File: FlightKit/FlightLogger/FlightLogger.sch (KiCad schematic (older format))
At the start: 14 parts, among them P101 CONN_2, P102 CONN_9, P103 CONN_4, P104 CONN_4

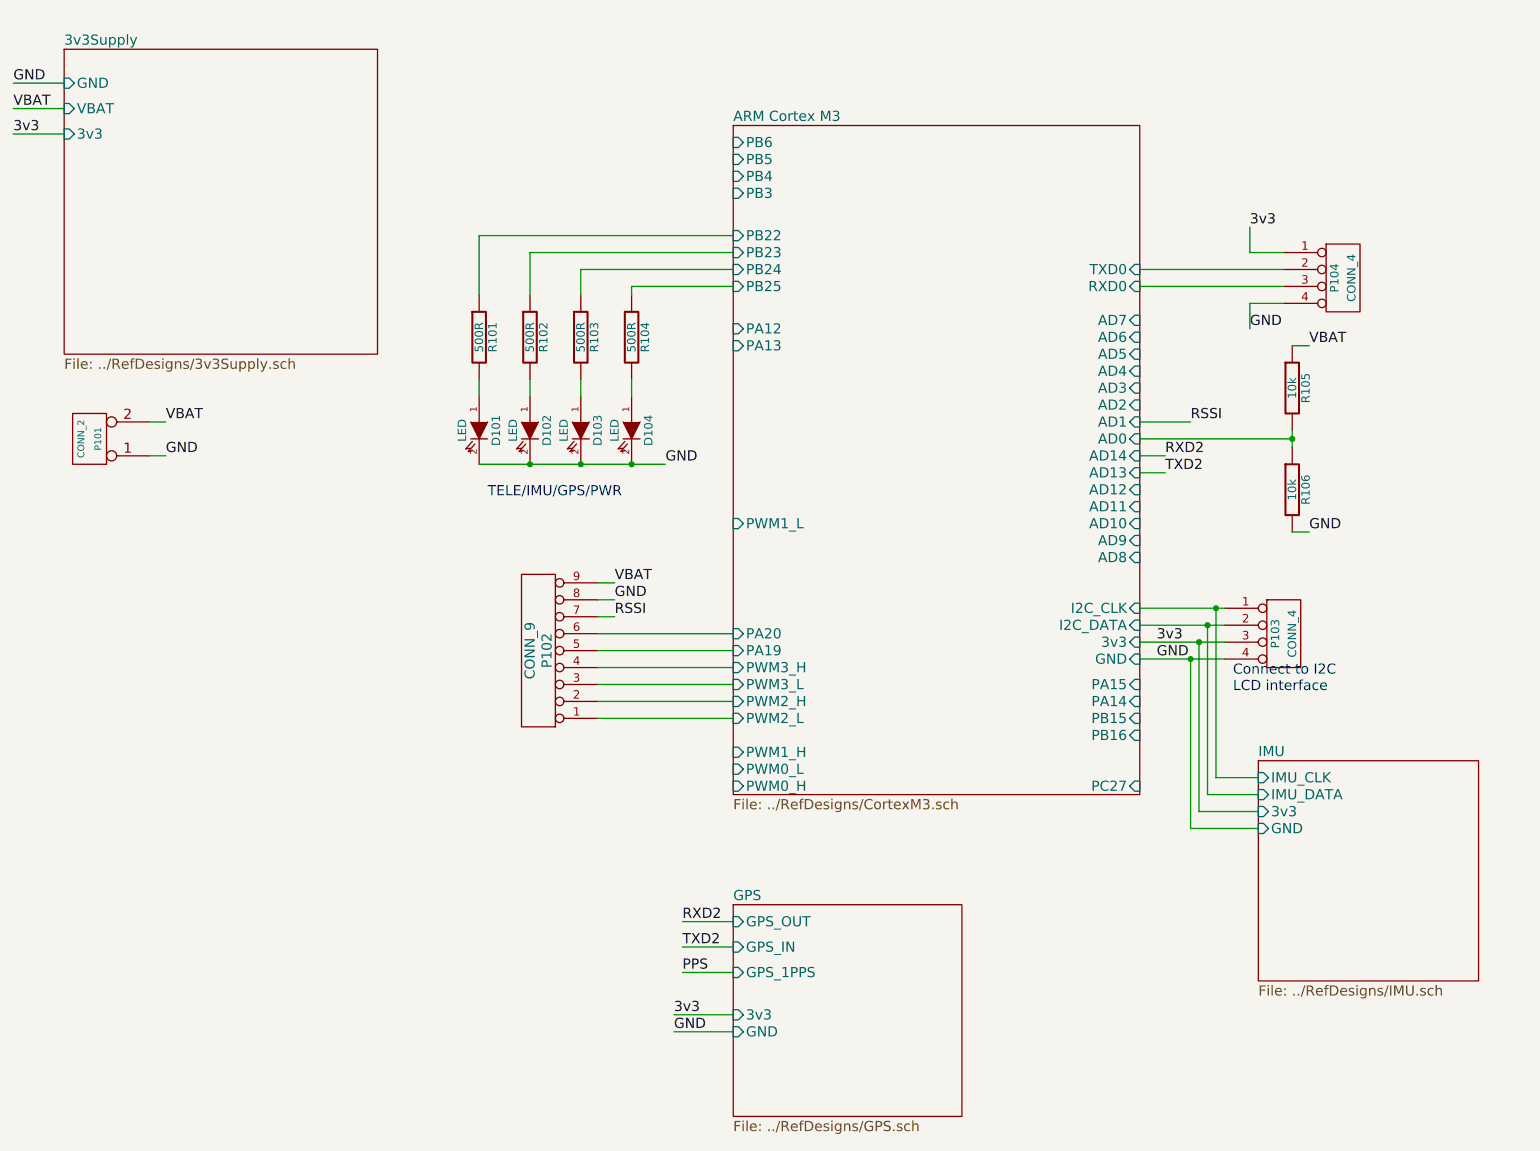
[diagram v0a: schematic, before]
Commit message: Added a digital input header. Remove pull-ups to use as digital outputs
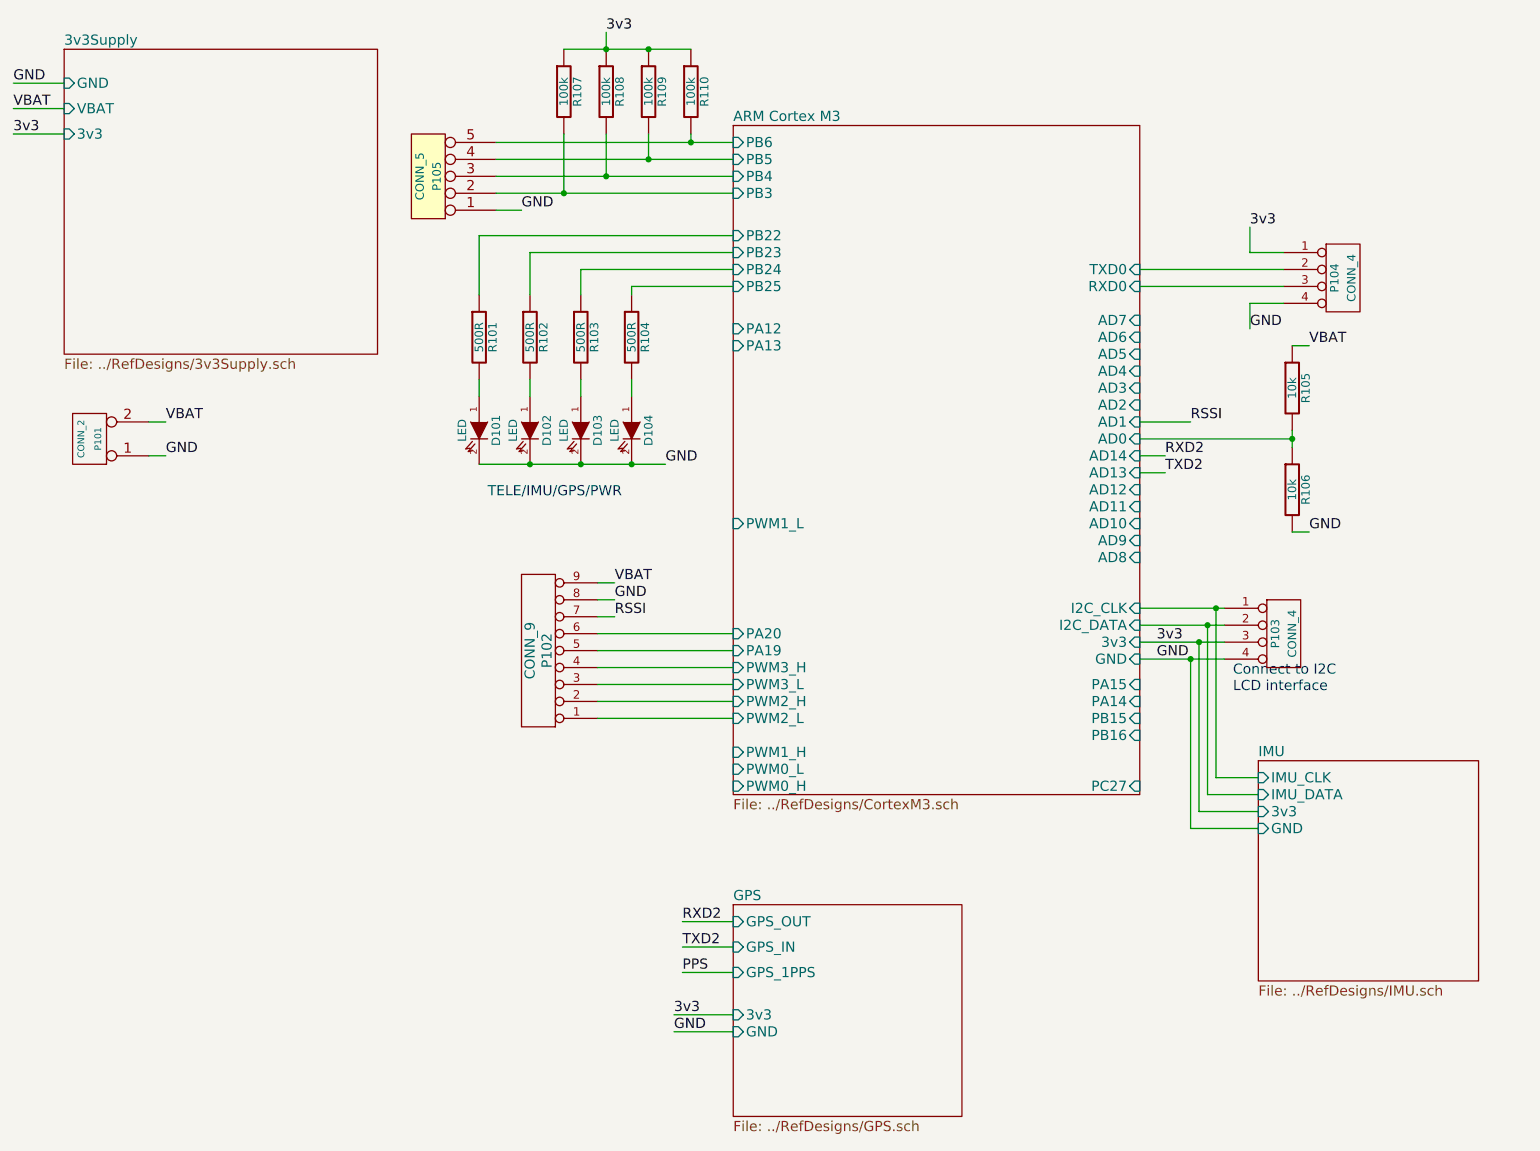
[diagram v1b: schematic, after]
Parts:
- added P105: CONN_5, symbol CONN_5
- added R107, R108, R109, R110: 100k, symbol R
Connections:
- net 3v3: now also R107.1, R108.1, R109.1, R110.1
- net ARM Cortex M3/PB3: now also P105.2, R107.2
- net ARM Cortex M3/PB4: now also P105.3, R108.2
- net ARM Cortex M3/PB5: now also P105.4, R109.2
- net ARM Cortex M3/PB6: now also P105.5, R110.2
- net GND: now also P105.1
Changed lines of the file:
@@
-EESchema Schematic File Version 2  date Tue 30 Jul 2013 17:36:58 BST
+EESchema Schematic File Version 2  date Fri 02 Aug 2013 09:19:04 BST
 LIBS:power
 LIBS:device
@@
 Sheet 1 5
 Title ""
-Date "30 jul 2013"
+Date "2 aug 2013"
 Rev ""
 Comp ""
@@
 Comment4 ""
 $EndDescr
+Connection ~ 4450 700
+Wire Wire Line
+	4700 700  3950 700
+Connection ~ 4700 1250
+Wire Wire Line
+	4700 1200 4700 1250
+Connection ~ 4200 1450
+Wire Wire Line
+	4200 1200 4200 1450
+Wire Wire Line
+	4950 1550 3550 1550
+Wire Wire Line
+	4950 1350 3550 1350
+Wire Wire Line
+	3550 1650 3700 1650
+Wire Wire Line
+	7350 3100 7500 3100
+Wire Wire Line
+	7350 2000 8200 2000
+Wire Wire Line
+	1500 2900 1600 2900
+Connection ~ 7700 4200
+Wire Wire Line
+	8050 5200 7700 5200
+Wire Wire Line
+	7700 5200 7700 4200
+Connection ~ 7800 4000
+Wire Wire Line
+	8050 5000 7800 5000
+Wire Wire Line
+	7800 5000 7800 4000
+Wire Wire Line
+	4150 4550 4950 4550
+Wire Wire Line
+	4150 4350 4950 4350
+Wire Wire Line
+	4150 4150 4950 4150
+Wire Wire Line
+	4150 3950 4250 3950
+Wire Wire Line
+	7350 4000 7850 4000
+Wire Wire Line
+	7850 4200 7350 4200
+Wire Wire Line
+	7350 4300 7850 4300
+Wire Wire Line
+	4950 1900 3750 1900
+Wire Wire Line
+	4950 2100 4350 2100
+Wire Wire Line
+	4650 6000 4950 6000
+Wire Wire Line
+	4600 6400 4950 6400
+Wire Wire Line
+	3450 2150 3450 1800
+Wire Wire Line
+	4050 2150 4050 2000
+Wire Wire Line
+	3450 2650 3450 2750
+Connection ~ 4050 3150
+Wire Wire Line
+	4350 2100 4350 2150
+Wire Wire Line
+	4050 2650 4050 2750
+Wire Wire Line
+	7350 2900 7650 2900
+Wire Wire Line
+	8250 2450 8350 2450
+Wire Wire Line
+	8250 2950 8250 3050
+Wire Wire Line
+	8200 2200 8000 2200
+Wire Wire Line
+	8000 2200 8000 2350
+Wire Wire Line
+	700  1200 1000 1200
+Wire Wire Line
+	700  900  1000 900
+Wire Wire Line
+	700  1050 1000 1050
+Wire Wire Line
+	8000 1750 8000 1900
+Wire Wire Line
+	8000 1900 8200 1900
+Wire Wire Line
+	8250 3000 7350 3000
+Connection ~ 8250 3000
+Wire Wire Line
+	8250 3550 8350 3550
+Wire Wire Line
+	4350 2650 4350 2750
+Wire Wire Line
+	3750 2650 3750 2750
+Connection ~ 4350 3150
+Wire Wire Line
+	3450 3150 4550 3150
+Connection ~ 3750 3150
+Wire Wire Line
+	3750 1900 3750 2150
+Wire Wire Line
+	4600 6500 4950 6500
+Wire Wire Line
+	4650 5850 4950 5850
+Wire Wire Line
+	4650 6150 4950 6150
+Wire Wire Line
+	4050 2000 4950 2000
+Wire Wire Line
+	3450 1800 4950 1800
+Wire Wire Line
+	7350 4100 7850 4100
+Wire Wire Line
+	4150 4050 4250 4050
+Wire Wire Line
+	4150 3850 4250 3850
+Wire Wire Line
+	4150 4250 4950 4250
+Wire Wire Line
+	4150 4450 4950 4450
+Wire Wire Line
+	4150 4650 4950 4650
+Wire Wire Line
+	7750 4100 7750 5100
+Wire Wire Line
+	7750 5100 8050 5100
+Connection ~ 7750 4100
+Wire Wire Line
+	7650 4300 7650 5300
+Wire Wire Line
+	7650 5300 8050 5300
+Connection ~ 7650 4300
+Wire Wire Line
+	1500 3100 1600 3100
+Wire Wire Line
+	8200 2100 7350 2100
 Wire Wire Line
 	7500 3200 7350 3200
 Wire Wire Line
-	8200 2100 7350 2100
-Wire Wire Line
-	1500 3100 1600 3100
-Connection ~ 7650 4300
-Wire Wire Line
-	8050 5300 7650 5300
-Wire Wire Line
-	7650 5300 7650 4300
-Connection ~ 7750 4100
-Wire Wire Line
-	8050 5100 7750 5100
-Wire Wire Line
-	7750 5100 7750 4100
-Wire Wire Line
-	4150 4650 4950 4650
-Wire Wire Line
-	4150 4450 4950 4450
-Wire Wire Line
-	4150 4250 4950 4250
-Wire Wire Line
-	4150 3850 4250 3850
-Wire Wire Line
-	4150 4050 4250 4050
-Wire Wire Line
-	7350 4100 7850 4100
-Wire Wire Line
-	4950 1800 3450 1800
-Wire Wire Line
-	4950 2000 4050 2000
-Wire Wire Line
-	4650 6150 4950 6150
-Wire Wire Line
-	4650 5850 4950 5850
-Wire Wire Line
-	4600 6500 4950 6500
-Wire Wire Line
-	3750 2150 3750 1900
-Connection ~ 3750 3150
-Wire Wire Line
-	3450 3150 4550 3150
-Connection ~ 4350 3150
-Wire Wire Line
-	3750 2650 3750 2750
-Wire Wire Line
-	4350 2650 4350 2750
-Wire Wire Line
-	8250 3550 8350 3550
-Connection ~ 8250 3000
-Wire Wire Line
-	8250 3000 7350 3000
-Wire Wire Line
-	8200 1900 8000 1900
-Wire Wire Line
-	8000 1900 8000 1750
-Wire Wire Line
-	700  1050 1000 1050
-Wire Wire Line
-	700  900  1000 900
-Wire Wire Line
-	700  1200 1000 1200
-Wire Wire Line
-	8000 2350 8000 2200
-Wire Wire Line
-	8000 2200 8200 2200
-Wire Wire Line
-	8250 2950 8250 3050
-Wire Wire Line
-	8250 2450 8350 2450
-Wire Wire Line
-	7350 2900 7650 2900
-Wire Wire Line
-	4050 2650 4050 2750
-Wire Wire Line
-	4350 2150 4350 2100
-Connection ~ 4050 3150
-Wire Wire Line
-	3450 2650 3450 2750
-Wire Wire Line
-	4050 2000 4050 2150
-Wire Wire Line
-	3450 1800 3450 2150
-Wire Wire Line
-	4600 6400 4950 6400
-Wire Wire Line
-	4650 6000 4950 6000
-Wire Wire Line
-	4350 2100 4950 2100
-Wire Wire Line
-	3750 1900 4950 1900
-Wire Wire Line
-	7350 4300 7850 4300
-Wire Wire Line
-	7850 4200 7350 4200
-Wire Wire Line
-	7350 4000 7850 4000
-Wire Wire Line
-	4150 3950 4250 3950
-Wire Wire Line
-	4150 4150 4950 4150
-Wire Wire Line
-	4150 4350 4950 4350
-Wire Wire Line
-	4150 4550 4950 4550
-Wire Wire Line
-	7800 4000 7800 5000
-Wire Wire Line
-	7800 5000 8050 5000
-Connection ~ 7800 4000
-Wire Wire Line
-	7700 4200 7700 5200
-Wire Wire Line
-	7700 5200 8050 5200
-Connection ~ 7700 4200
-Wire Wire Line
-	1500 2900 1600 2900
-Wire Wire Line
-	7350 2000 8200 2000
-Wire Wire Line
-	7350 3100 7500 3100
+	3550 1250 4950 1250
+Wire Wire Line
+	3550 1450 4950 1450
+Wire Wire Line
+	3950 1200 3950 1550
+Connection ~ 3950 1550
+Wire Wire Line
+	4450 1200 4450 1350
+Connection ~ 4450 1350
+Wire Wire Line
+	4200 700  4200 600
+Connection ~ 4200 700
+Text Label 3700 1650 0    60   ~ 0
+GND
+$Comp
+L CONN_5 P105
+U 1 1 51FB6B32
+P 3150 1450
+F 0 "P105" V 3100 1450 50  0000 C CNN
+F 1 "CONN_5" V 3200 1450 50  0000 C CNN
+	1    3150 1450
+	-1   0    0    1
+$EndComp
+$Comp
+L R R107
+U 1 1 51FB6B20
+P 3950 950
+F 0 "R107" V 4030 950 50  0000 C CNN
+F 1 "100k" V 3950 950 50  0000 C CNN
+	1    3950 950
+	1    0    0    -1
+$EndComp
+$Comp
+L R R110
+U 1 1 51FB6B1B
+P 4700 950
+F 0 "R110" V 4780 950 50  0000 C CNN
+F 1 "100k" V 4700 950 50  0000 C CNN
+	1    4700 950
+	1    0    0    -1
+$EndComp
+$Comp
+L R R109
+U 1 1 51FB6B14
+P 4450 950
+F 0 "R109" V 4530 950 50  0000 C CNN
+F 1 "100k" V 4450 950 50  0000 C CNN
+	1    4450 950
+	1    0    0    -1
+$EndComp
+$Comp
+L R R108
+U 1 1 51FB6B03
+P 4200 950
+F 0 "R108" V 4280 950 50  0000 C CNN
+F 1 "100k" V 4200 950 50  0000 C CNN
+	1    4200 950
+	1    0    0    -1
+$EndComp
+Text Label 4200 600  0    60   ~ 0
+3v3
 $Sheet
 S 4950 1150 2400 3950
